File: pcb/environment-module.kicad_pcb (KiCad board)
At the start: 4 copper layers, 50 x 25 mm, 109 parts, among them J1 AVR-UPDI-6, U1 ATtiny1616-MNR, U2 PCA9545APW, U3 AHT20-F, U4 LTR-303ALS-01, U5 SGP40-D-R4

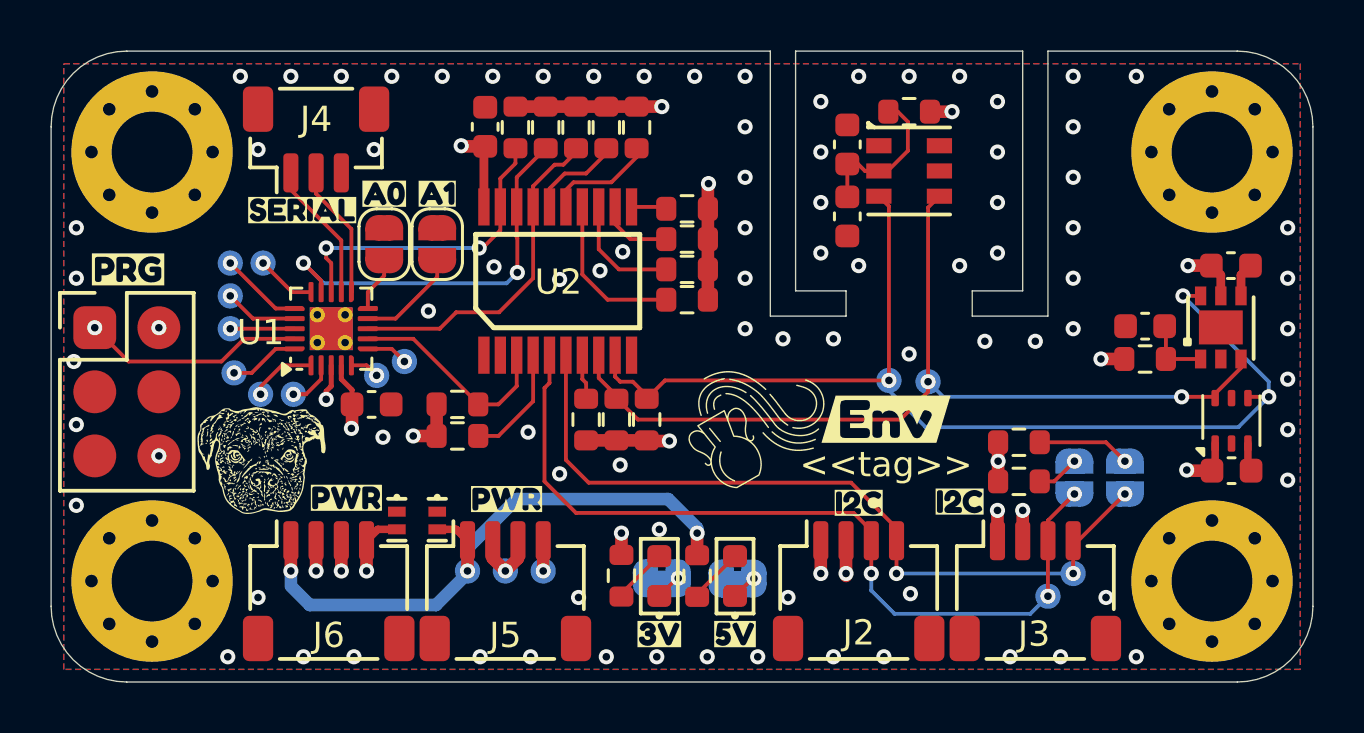
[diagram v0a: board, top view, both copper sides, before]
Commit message: Added labels for sensors
Fixed part numbers for connectors
Remove unnecessary property values
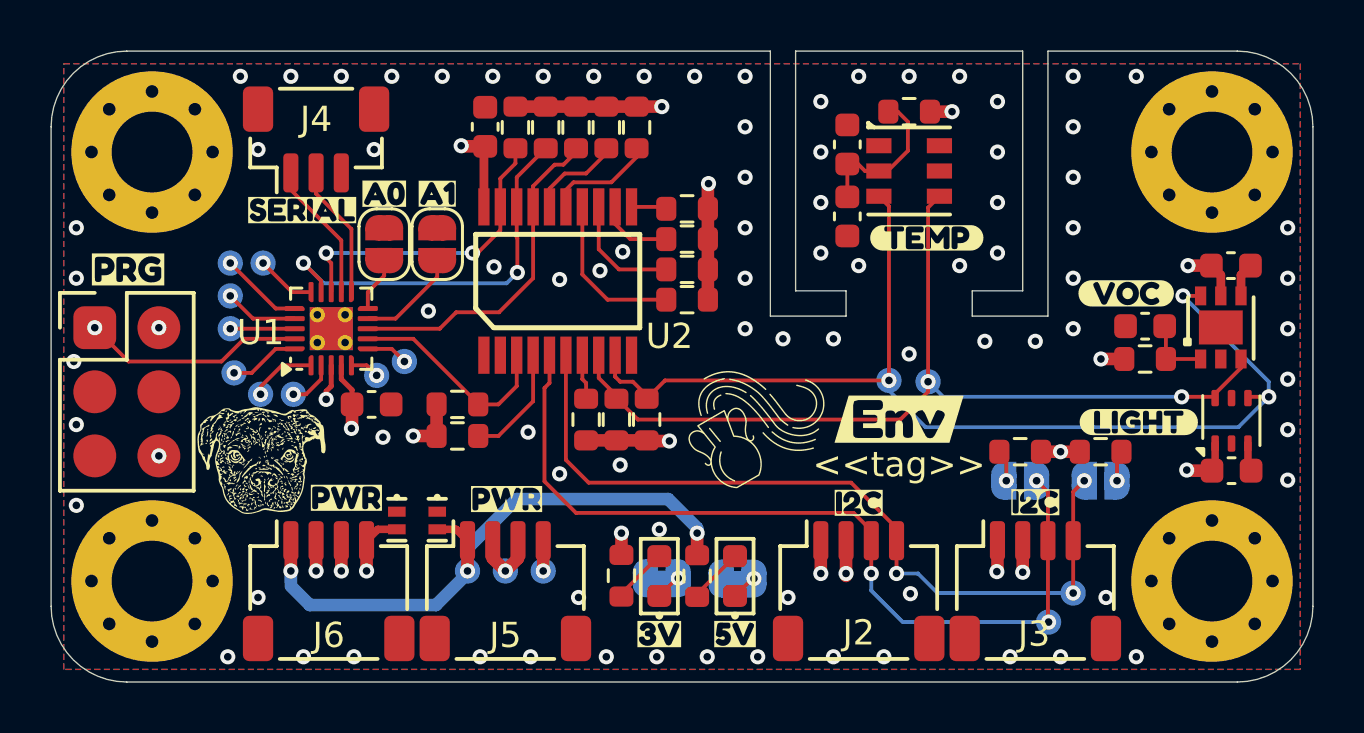
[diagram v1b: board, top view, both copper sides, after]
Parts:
- added kibuzzard-6952D1DF: G***, kibuzzard-6952D1DF, F.Cu at (84.7, 132.4)
- added kibuzzard-6952D1FF: G***, kibuzzard-6952D1FF, F.Cu at (93.1, 139.7)
- added kibuzzard-6952D20C: G***, kibuzzard-6952D20C, F.Cu at (92.6, 134.6)
- moved kibuzzard-68F7F6D5 4.53 mm to (86.5, 142.0)
- moved R2 3.26 mm to (91.6, 140.9)
- moved kibuzzard-68FAFCDC 3.00 mm to (89.0, 142.9)
- moved kibuzzard-68F7F6E1 2.33 mm to (93.5, 141.9)
- moved JP4 2.15 mm to (88.4, 142.0), turned to 180 degrees
- moved kibuzzard-690D6835 1.35 mm to (88.9, 144.7), turned to 135 degrees
- moved R3 1.18 mm to (88.4, 140.9), turned to 0 degrees
- moved TP14 1.03 mm to (89.5, 147.6)
- moved JP3 0.97 mm to (91.6, 142.0), turned to 0 degrees
- moved TP13 0.78 mm to (90.5, 146.5)
- moved kibuzzard-690D683A 0.76 mm to (86.9, 147.6)
- moved kibuzzard-69029C60 0.52 mm to (83.6, 139.6)
- moved LOGO1 0.46 mm to (74.5, 136.8)
- moved kibuzzard-691D233B 0.46 mm to (68.7, 135.8)
- moved LOGO7 0.36 mm to (84.0, 141.9)
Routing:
- net Net-(JP3-B): track 3.69 -> 0.97 mm
- net EXT_SDA: track 33.5 -> 34.7 mm
- net EXT_SCL: track 31.2 -> 32.2 mm
- net Net-(JP4-B): track 1.71 -> 0.88 mm
